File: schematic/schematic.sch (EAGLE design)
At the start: 10 parts, among them J2 SJ-2523-SMT-TR

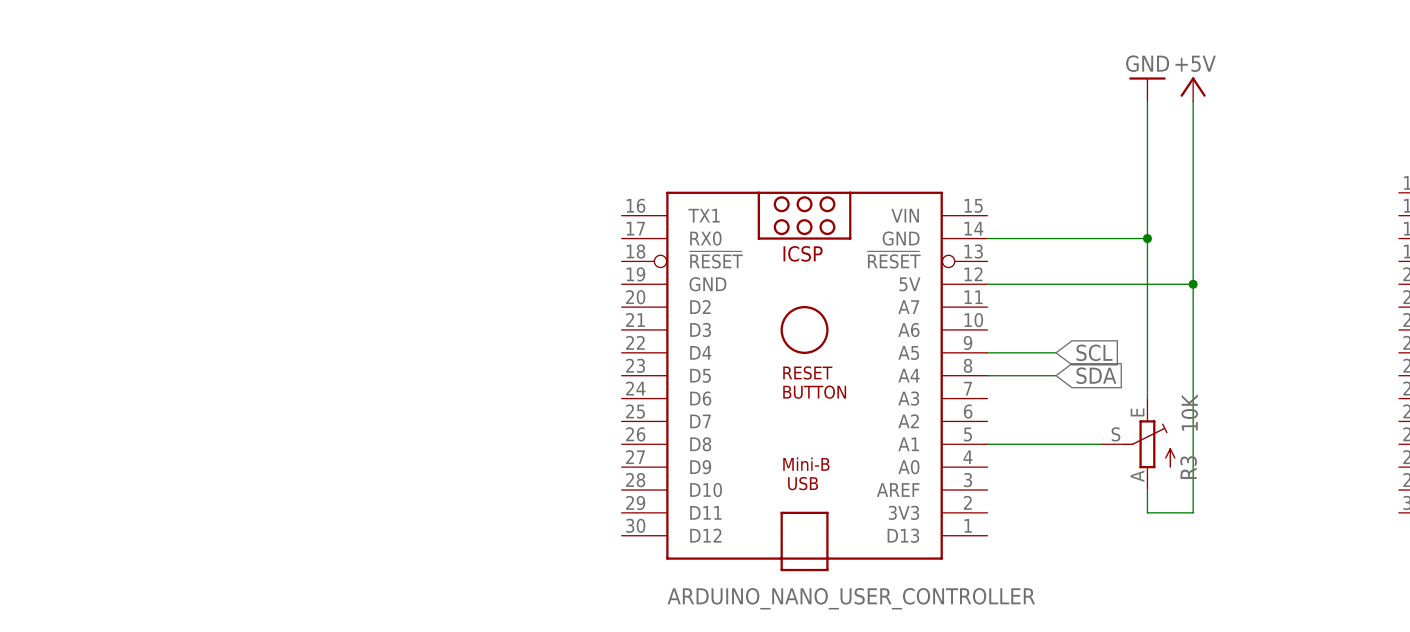
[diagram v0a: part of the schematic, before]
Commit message: Add volume potentiometer to schematic
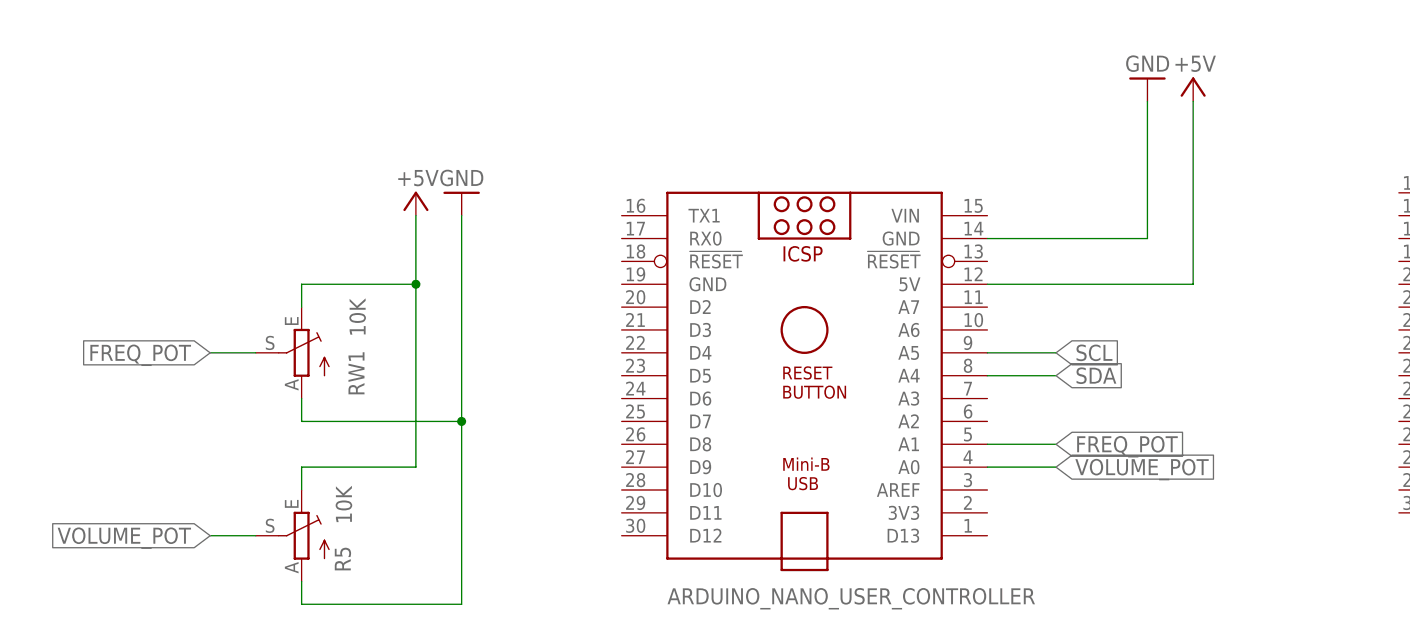
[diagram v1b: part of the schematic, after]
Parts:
- removed R3: 10K, pot:TRIM_EU-B25V
- added R5, RW1: 10K, pot:TRIM_EU-B25V
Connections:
- removed net N$4: ARDUINO_NANO_USER_CONTROLLER.A0, ARDUINO_NANO_USER_CONTROLLER.A1, R3.S
- new net FREQ_POT: ARDUINO_NANO_USER_CONTROLLER.A1, RW1.S
- new net VOLUME_POT: ARDUINO_NANO_USER_CONTROLLER.A0, R5.S
- net +5V: now also R5.E, RW1.E; no longer R3.A
- net GND: now also R5.A, RW1.A; no longer R3.E
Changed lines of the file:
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@@
 <schematic_group name="RADIO_MODULE"/>
 <schematic_group name="POWER_FILTRATION"/>
+<schematic_group name="CONTROLLERS"/>
 </groups>
 <parts>
@@
 <part name="J2" library="Audio Connectors" library_urn="urn:adsk.eagle:library:16251796" deviceset="SJ-2523-SMT-TR" device="" package3d_urn="urn:adsk.eagle:package:16225688/4"/>
 <part name="+3V1" library="supply1" library_urn="urn:adsk.eagle:library:371" deviceset="+3V3" device=""/>
-<part name="R3" library="pot" library_urn="urn:adsk.eagle:library:331" deviceset="TRIM_EU-" device="B25V" package3d_urn="urn:adsk.eagle:package:22683/1" value="10K"/>
 <part name="C2" library="rcl" library_urn="urn:adsk.eagle:library:334" deviceset="C-EU" device="025-024X044" package3d_urn="urn:adsk.eagle:package:23630/1" value="100n"/>
 <part name="C1" library="rcl" library_urn="urn:adsk.eagle:library:334" deviceset="CPOL-EU" device="E2,5-6E" package3d_urn="urn:adsk.eagle:package:23430/1" value="22u"/>
 <part name="P+2" library="supply1" library_urn="urn:adsk.eagle:library:371" deviceset="+5V" device=""/>
 <part name="GND4" library="supply1" library_urn="urn:adsk.eagle:library:371" deviceset="GND" device=""/>
+<part name="RW1" library="pot" library_urn="urn:adsk.eagle:library:331" deviceset="TRIM_EU-" device="B25V" package3d_urn="urn:adsk.eagle:package:22683/1" value="10K"/>
+<part name="R5" library="pot" library_urn="urn:adsk.eagle:library:331" deviceset="TRIM_EU-" device="B25V" package3d_urn="urn:adsk.eagle:package:22683/1" value="10K"/>
+<part name="GND5" library="supply1" library_urn="urn:adsk.eagle:library:371" deviceset="GND" device=""/>
+<part name="P+5" library="supply1" library_urn="urn:adsk.eagle:library:371" deviceset="+5V" device=""/>
 </parts>
 <sheets>
@@
 <attribute name="VALUE" x="50.8" y="99.06" size="1.778" layer="96"/>
 </instance>
-<instance part="R3" gate="1" x="40.64" y="38.1" smashed="yes" rot="MR0" grouprefs="USER_CONTROLLER">
-<attribute name="NAME" x="44.323" y="34.036" size="1.778" layer="95" rot="MR90"/>
-<attribute name="VALUE" x="44.45" y="39.37" size="1.778" layer="96" rot="MR90"/>
-</instance>
 <instance part="C2" gate="G$1" x="-31.75" y="115.3668" smashed="yes" grouprefs="POWER_FILTRATION">
 <attribute name="NAME" x="-30.226" y="115.7478" size="1.778" layer="95"/>
@@
 <instance part="GND4" gate="1" x="-26.67" y="100.1268" smashed="yes" grouprefs="POWER_FILTRATION">
 <attribute name="VALUE" x="-29.21" y="97.5868" size="1.778" layer="96"/>
+</instance>
+<instance part="RW1" gate="1" x="-53.34" y="48.26" smashed="yes" rot="MR0" grouprefs="CONTROLLERS">
+<attribute name="NAME" x="-48.133" y="43.434" size="1.778" layer="95" rot="MR90"/>
+<attribute name="VALUE" x="-48.006" y="50.038" size="1.778" layer="96" rot="MR90"/>
+</instance>
+<instance part="R5" gate="1" x="-53.34" y="27.94" smashed="yes" rot="MR0" grouprefs="CONTROLLERS">
+<attribute name="NAME" x="-49.657" y="23.876" size="1.778" layer="95" rot="MR90"/>
+<attribute name="VALUE" x="-49.53" y="29.21" size="1.778" layer="96" rot="MR90"/>
+</instance>
+<instance part="GND5" gate="1" x="-35.56" y="66.04" smashed="yes" rot="R180" grouprefs="CONTROLLERS">
+<attribute name="VALUE" x="-33.02" y="68.58" size="1.778" layer="96" rot="R180"/>
+</instance>
+<instance part="P+5" gate="1" x="-40.64" y="66.04" smashed="yes" grouprefs="CONTROLLERS">
+<attribute name="VALUE" x="-38.1" y="68.58" size="1.778" layer="96" rot="R180"/>
 </instance>
 </instances>
@@
 <wire x1="40.64" y1="76.2" x2="40.64" y2="60.96" width="0.1524" layer="91" grouprefs="USER_CONTROLLER"/>
 <wire x1="40.64" y1="60.96" x2="22.86" y2="60.96" width="0.1524" layer="91" grouprefs="USER_CONTROLLER"/>
-<pinref part="R3" gate="1" pin="E"/>
-<wire x1="40.64" y1="60.96" x2="40.64" y2="43.18" width="0.1524" layer="91" grouprefs="USER_CONTROLLER"/>
-<junction x="40.64" y="60.96" grouprefs="USER_CONTROLLER"/>
 </segment>
 <segment>
@@
 <junction x="-26.67" y="107.7468" grouprefs="POWER_FILTRATION"/>
 </segment>
+<segment>
+<pinref part="R5" gate="1" pin="A"/>
+<wire x1="-53.34" y1="22.86" x2="-53.34" y2="20.32" width="0.1524" layer="91" grouprefs="CONTROLLERS"/>
+<pinref part="GND5" gate="1" pin="GND"/>
+<wire x1="-53.34" y1="20.32" x2="-35.56" y2="20.32" width="0.1524" layer="91" grouprefs="CONTROLLERS"/>
+<wire x1="-35.56" y1="20.32" x2="-35.56" y2="40.64" width="0.1524" layer="91" grouprefs="CONTROLLERS"/>
+<pinref part="RW1" gate="1" pin="A"/>
+<wire x1="-35.56" y1="40.64" x2="-35.56" y2="63.5" width="0.1524" layer="91" grouprefs="CONTROLLERS"/>
+<wire x1="-53.34" y1="43.18" x2="-53.34" y2="40.64" width="0.1524" layer="91" grouprefs="CONTROLLERS"/>
+<wire x1="-53.34" y1="40.64" x2="-35.56" y2="40.64" width="0.1524" layer="91" grouprefs="CONTROLLERS"/>
+<junction x="-35.56" y="40.64" grouprefs="CONTROLLERS"/>
+</segment>
 </net>
 <net name="+5V" class="0">
@@
 <wire x1="45.72" y1="76.2" x2="45.72" y2="55.88" width="0.1524" layer="91" grouprefs="USER_CONTROLLER"/>
 <wire x1="45.72" y1="55.88" x2="22.86" y2="55.88" width="0.1524" layer="91" grouprefs="USER_CONTROLLER"/>
-<pinref part="R3" gate="1" pin="A"/>
-<wire x1="40.64" y1="33.02" x2="40.64" y2="30.48" width="0.1524" layer="91" grouprefs="USER_CONTROLLER"/>
-<wire x1="40.64" y1="30.48" x2="45.72" y2="30.48" width="0.1524" layer="91" grouprefs="USER_CONTROLLER"/>
-<wire x1="45.72" y1="30.48" x2="45.72" y2="55.88" width="0.1524" layer="91" grouprefs="USER_CONTROLLER"/>
-<junction x="45.72" y="55.88" grouprefs="USER_CONTROLLER"/>
 </segment>
 <segment>
@@
 <junction x="-26.67" y="120.4468" grouprefs="POWER_FILTRATION"/>
 </segment>
+<segment>
+<pinref part="P+5" gate="1" pin="+5V"/>
+<wire x1="-40.64" y1="63.5" x2="-40.64" y2="55.88" width="0.1524" layer="91" grouprefs="CONTROLLERS"/>
+<pinref part="R5" gate="1" pin="E"/>
+<wire x1="-40.64" y1="55.88" x2="-40.64" y2="35.56" width="0.1524" layer="91" grouprefs="CONTROLLERS"/>
+<wire x1="-53.34" y1="33.02" x2="-53.34" y2="35.56" width="0.1524" layer="91" grouprefs="CONTROLLERS"/>
+<wire x1="-53.34" y1="35.56" x2="-40.64" y2="35.56" width="0.1524" layer="91" grouprefs="CONTROLLERS"/>
+<pinref part="RW1" gate="1" pin="E"/>
+<wire x1="-53.34" y1="53.34" x2="-53.34" y2="55.88" width="0.1524" layer="91" grouprefs="CONTROLLERS"/>
+<wire x1="-53.34" y1="55.88" x2="-40.64" y2="55.88" width="0.1524" layer="91" grouprefs="CONTROLLERS"/>
+<junction x="-40.64" y="55.88" grouprefs="CONTROLLERS"/>
+</segment>
 </net>
 <net name="N$1" class="0">
@@
 </segment>
 </net>
-<net name="N$4" class="0">
+<net name="FREQ_POT" class="0">
+<segment>
+<pinref part="RW1" gate="1" pin="S"/>
+<wire x1="-58.42" y1="48.26" x2="-63.5" y2="48.26" width="0.1524" layer="91" grouprefs="CONTROLLERS"/>
+<label x="-63.5" y="48.26" size="1.778" layer="95" rot="R180" xref="yes" grouprefs="CONTROLLERS"/>
+</segment>
+<segment>
+<pinref part="ARDUINO_NANO_USER_CONTROLLER" gate="G$1" pin="A1"/>
+<wire x1="22.86" y1="38.1" x2="30.48" y2="38.1" width="0.1524" layer="91"/>
+<label x="30.48" y="38.1" size="1.778" layer="95" xref="yes"/>
+</segment>
+</net>
+<net name="VOLUME_POT" class="0">
+<segment>
+<pinref part="R5" gate="1" pin="S"/>
+<wire x1="-58.42" y1="27.94" x2="-63.5" y2="27.94" width="0.1524" layer="91" grouprefs="CONTROLLERS"/>
+<label x="-63.5" y="27.94" size="1.778" layer="95" rot="R180" xref="yes" grouprefs="CONTROLLERS"/>
+</segment>
 <segment>
 <pinref part="ARDUINO_NANO_USER_CONTROLLER" gate="G$1" pin="A0"/>
-<pinref part="R3" gate="1" pin="S"/>
-<wire x1="22.86" y1="38.1" x2="35.56" y2="38.1" width="0.1524" layer="91" grouprefs="USER_CONTROLLER"/>
-<pinref part="ARDUINO_NANO_USER_CONTROLLER" gate="G$1" pin="A1"/>
-</segment>
-</net>
+<wire x1="22.86" y1="35.56" x2="30.48" y2="35.56" width="0.1524" layer="91"/>
+<label x="30.48" y="35.56" size="1.778" layer="95" xref="yes"/>
+</segment>
+</net>

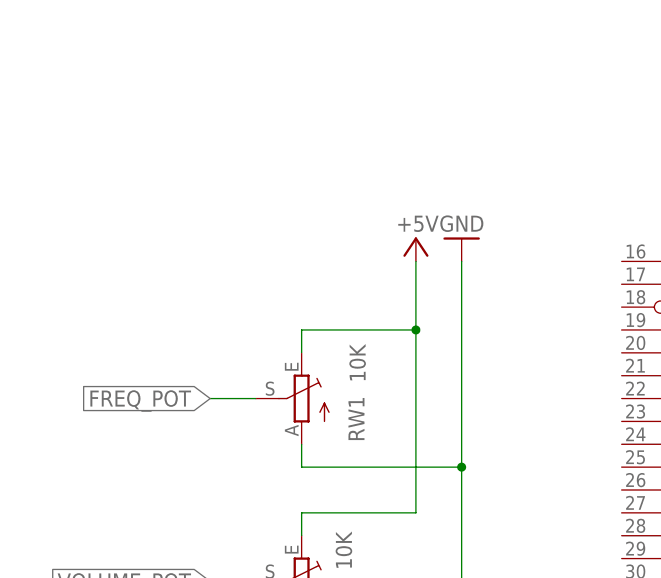
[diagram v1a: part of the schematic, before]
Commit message: Add capacitor for frequency potentiometer
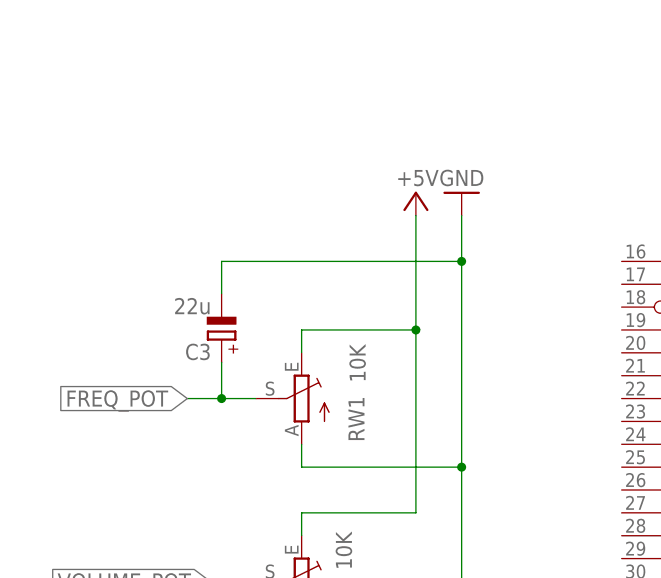
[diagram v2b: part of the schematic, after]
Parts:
- added C3: 22u, rcl:CPOL-EUE2,5-6E
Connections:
- net FREQ_POT: now also C3.+
- net GND: now also C3.-
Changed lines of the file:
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@@
 <part name="GND5" library="supply1" library_urn="urn:adsk.eagle:library:371" deviceset="GND" device=""/>
 <part name="P+5" library="supply1" library_urn="urn:adsk.eagle:library:371" deviceset="+5V" device=""/>
+<part name="C3" library="rcl" library_urn="urn:adsk.eagle:library:334" deviceset="CPOL-EU" device="E2,5-6E" package3d_urn="urn:adsk.eagle:package:23430/1" value="22u"/>
 </parts>
 <sheets>
@@
 <attribute name="VALUE" x="-49.53" y="29.21" size="1.778" layer="96" rot="MR90"/>
 </instance>
-<instance part="GND5" gate="1" x="-35.56" y="66.04" smashed="yes" rot="R180" grouprefs="CONTROLLERS">
-<attribute name="VALUE" x="-33.02" y="68.58" size="1.778" layer="96" rot="R180"/>
-</instance>
-<instance part="P+5" gate="1" x="-40.64" y="66.04" smashed="yes" grouprefs="CONTROLLERS">
-<attribute name="VALUE" x="-38.1" y="68.58" size="1.778" layer="96" rot="R180"/>
+<instance part="GND5" gate="1" x="-35.56" y="71.12" smashed="yes" rot="R180" grouprefs="CONTROLLERS">
+<attribute name="VALUE" x="-33.02" y="73.66" size="1.778" layer="96" rot="R180"/>
+</instance>
+<instance part="P+5" gate="1" x="-40.64" y="71.12" smashed="yes" grouprefs="CONTROLLERS">
+<attribute name="VALUE" x="-38.1" y="73.66" size="1.778" layer="96" rot="R180"/>
+</instance>
+<instance part="C3" gate="G$1" x="-62.23" y="54.8132" smashed="yes" rot="R180">
+<attribute name="NAME" x="-63.373" y="54.3306" size="1.778" layer="95" rot="R180"/>
+<attribute name="VALUE" x="-63.373" y="59.4106" size="1.778" layer="96" rot="R180"/>
 </instance>
 </instances>
@@
 <pinref part="RW1" gate="1" pin="A"/>
 <wire x1="-35.56" y1="40.64" x2="-35.56" y2="63.5" width="0.1524" layer="91" grouprefs="CONTROLLERS"/>
+<wire x1="-35.56" y1="63.5" x2="-35.56" y2="68.58" width="0.1524" layer="91" grouprefs="CONTROLLERS"/>
 <wire x1="-53.34" y1="43.18" x2="-53.34" y2="40.64" width="0.1524" layer="91" grouprefs="CONTROLLERS"/>
 <wire x1="-53.34" y1="40.64" x2="-35.56" y2="40.64" width="0.1524" layer="91" grouprefs="CONTROLLERS"/>
 <junction x="-35.56" y="40.64" grouprefs="CONTROLLERS"/>
+<pinref part="C3" gate="G$1" pin="-"/>
+<wire x1="-62.23" y1="59.8932" x2="-62.23" y2="63.5" width="0.1524" layer="91"/>
+<wire x1="-62.23" y1="63.5" x2="-35.56" y2="63.5" width="0.1524" layer="91"/>
+<junction x="-35.56" y="63.5"/>
 </segment>
 </net>
@@
 <segment>
 <pinref part="P+5" gate="1" pin="+5V"/>
-<wire x1="-40.64" y1="63.5" x2="-40.64" y2="55.88" width="0.1524" layer="91" grouprefs="CONTROLLERS"/>
+<wire x1="-40.64" y1="68.58" x2="-40.64" y2="55.88" width="0.1524" layer="91" grouprefs="CONTROLLERS"/>
 <pinref part="R5" gate="1" pin="E"/>
 <wire x1="-40.64" y1="55.88" x2="-40.64" y2="35.56" width="0.1524" layer="91" grouprefs="CONTROLLERS"/>
@@
 <segment>
 <pinref part="RW1" gate="1" pin="S"/>
-<wire x1="-58.42" y1="48.26" x2="-63.5" y2="48.26" width="0.1524" layer="91" grouprefs="CONTROLLERS"/>
-<label x="-63.5" y="48.26" size="1.778" layer="95" rot="R180" xref="yes" grouprefs="CONTROLLERS"/>
-</segment>
-<segment>
+<wire x1="-58.42" y1="48.26" x2="-62.23" y2="48.26" width="0.1524" layer="91" grouprefs="CONTROLLERS"/>
+<label x="-66.04" y="48.26" size="1.778" layer="95" rot="R180" xref="yes" grouprefs="CONTROLLERS"/>
+<pinref part="C3" gate="G$1" pin="+"/>
+<wire x1="-62.23" y1="48.26" x2="-66.04" y2="48.26" width="0.1524" layer="91" grouprefs="CONTROLLERS"/>
+<wire x1="-62.23" y1="52.2732" x2="-62.23" y2="48.26" width="0.1524" layer="91"/>
+<junction x="-62.23" y="48.26"/>
+</segment>
+<segment>
